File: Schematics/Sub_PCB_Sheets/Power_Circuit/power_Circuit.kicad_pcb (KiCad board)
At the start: 2 copper layers, 494.6 x 179.4 mm, 277 parts, among them IC1 F280049CPMSR, IC2 CP2102N-A02-GQFN24R, IC3 TPD2EUSB30ADRTR, J1 23AH8786-Red, J10 464379202, J11 464369202, J12 464379202, J13 43045-1212, J14 43650-0418, J15 43650-0418, J16 464369202, J17 464379202, J18 43650-0418, J19 FTSH-105-01-LM-D-K, J2 23AH8785-Black, J20 43045-1212, J21 43650-0418, J22 43650-0418, J23 464369202, J24 43650-0418, J25 43650-0418, J26 43650-0418, J27 43650-0418, J28 1051330011, J3 23AH8786-Red, J4 23AH8785-Black, J5 464379202, J6 464369202, J7 43650-0418, J8 464379202, J9 464369202, Q1 STB10NK60ZT4, Q2 C3M0025065K, Q3 C3M0025065K, Q4 C3M0025065K, Q5 C3M0025065K, Q6 PC817X1CSP9F, Q7 PC817X1CSP9F, Q8 STB10NK60ZT4, U1 UCC21710QDWRQ1, U2 UCC21710QDWRQ1, U3 UCC21710QDWRQ1, U4 UCC21710QDWRQ1, U5 TR05S3V3, Y1 ABM8-20.000MHZ-B2-T

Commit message: Power Board PCB completed and generated Feb output files
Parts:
- removed C1: 1 uF, SiC_Inverter:R71PI410050H6K
- removed C10, C12, C14, C15, C16, C2, C3, C4, C6, C8: 22 uF, SiC_Inverter:ESH226M500AL4AA
- removed C11, C13, C5, C7, C9: 2 uF, SiC_Inverter:MKP1848C52050JK2
- removed C17, C18, C35, C36: 15 uF, Capacitor_SMD:C_1206_3216Metric_Pad1.33x1.80mm_HandSolder
- removed C19, C20, C26, C29, C30, C33, C37, C38, C44, C47, C48, C51, C54, C55, C56, C57, C58, C60, C61, C62, C63, C66, C67: 0.1 uF, Capacitor_SMD:C_0805_2012Metric_Pad1.18x1.45mm_HandSolder
- removed C21, C22, C27, C34, C39, C40, C45, C52, C69: 1 uF, Capacitor_SMD:C_1206_3216Metric_Pad1.33x1.80mm_HandSolder
- removed C23, C24, C25, C28, C31, C32, C41, C42, C43, C46, C49, C50: 100 pF, Capacitor_SMD:C_0603_1608Metric_Pad1.08x0.95mm_HandSolder
- removed C53: 6.8 uF, SiC_Inverter:C4AF9BW4680T3FK
- removed C59, C68: 10 uF, Capacitor_SMD:C_0805_2012Metric_Pad1.18x1.45mm_HandSolder
- removed C64, C65: 18 pF, Capacitor_SMD:C_0402_1005Metric_Pad0.74x0.62mm_HandSolder
- removed D1, D7: BZX84C15-7-F, Package_TO_SOT_SMD:SOT-23-3
- removed D2, D3, D4, D5: BZX84C20-7-F, Package_TO_SOT_SMD:SOT-23-3
- removed D6: P6KE500A-HF, Diode_THT:D_DO-15_P12.70mm_Horizontal
- removed F1: 0031.8322, SiC_Inverter:0031.8322
- removed the G*** at (500.1, 162.0)
- removed the G*** at (67.5, 176.0)
- removed the G*** at (153.3, 177.6)
- removed the G*** at (299.4, 164.9)
- removed the G*** at (224.0, 180.9)
- removed the G*** at (382.6, 134.4)
- removed the G*** at (299.1, 62.0)
- removed H1, H13, H14, H15, H16, H17, H18, H19, H2, H20, H21, H22, H23, H24, H25, H26, H27, H28, H29, H3, H30, H31, H32, H4, H5, H6, H7, H8: MountingHole, MountingHole:MountingHole_2.2mm_M2
- removed IC1: F280049CPMSR, SiC_Inverter:F280049CPMSR
- removed IC2: CP2102N-A02-GQFN24R, SiC_Inverter:CP2102N-A02-GQFN24R
- removed IC3: TPD2EUSB30ADRTR, SiC_Inverter:TPD2EUSB30ADRTR
- removed J1, J3: 23AH8786-Red, SiC_Inverter:23AH8786-Red
- removed J10, J12, J17, J5, J8: 464379202, SiC_Inverter:46437-900_02
- removed J11, J16, J23, J6, J9: 464369202, SiC_Inverter:46436-900_02
- removed J13, J20: 43045-1212, SiC_Inverter:43045-1212
- removed J14, J15, J18, J21, J22, J24, J7: 43650-0418, SiC_Inverter:436500418
- removed J19: FTSH-105-01-LM-D-K, SiC_Inverter:FTSH-105-01-LM-D-K
- removed J2, J4: 23AH8785-Black, SiC_Inverter:23AH8785-Black
- removed J28: 1051330011, SiC_Inverter:105133-0011
- removed L1: 47 uH, SiC_Inverter:2300HT_470
- removed L2: 2.2 mH, SiC_Inverter:7448258022
- removed L3, L4: 470 uH, SiC_Inverter:1140471KRC
- removed Q1, Q8: STB10NK60ZT4, Package_TO_SOT_SMD:TO-263-2
- removed Q2, Q3, Q4, Q5: C3M0025065K, SiC_Inverter:C3M0025065K
- removed Q6, Q7: PC817X1CSP9F, SiC_Inverter:PC817X1CSP9F
- removed R1, R44, R45: 499 K, Resistor_SMD:R_1206_3216Metric_Pad1.30x1.75mm_HandSolder
- removed R10, R21, R22, R23, R24, R7, R8, R9: 10, Resistor_SMD:R_1206_3216Metric_Pad1.30x1.75mm_HandSolder
- removed R11, R13, R14, R16, R17, R18, R25, R27, R28, R30, R31, R32: 5 K, Resistor_SMD:R_1206_3216Metric_Pad1.30x1.75mm_HandSolder
- removed R12, R15, R26, R29: 100, Resistor_SMD:R_1206_3216Metric_Pad1.30x1.75mm_HandSolder
- removed R19, R20, R34, R36, R37, R39, R4, R40, R41, R43, R47, R48, R5, R6: 100 K, Resistor_SMD:R_1206_3216Metric_Pad1.30x1.75mm_HandSolder
- removed R2: CW005100R0JE12HE, SiC_Inverter:CW005100R0JE12HE
- removed R3, R46: 47, Resistor_SMD:R_1206_3216Metric_Pad1.30x1.75mm_HandSolder
- removed R33: 6, SiC_Inverter:CW005100R0JE12HE
- removed R35, R42: 10 K, Resistor_SMD:R_1206_3216Metric_Pad1.30x1.75mm_HandSolder
- removed R38: 2 K, Resistor_SMD:R_1206_3216Metric_Pad1.30x1.75mm_HandSolder
- removed R49: 0, Resistor_SMD:R_1206_3216Metric_Pad1.30x1.75mm_HandSolder
- removed TP1, TP11, TP24, TP25, TP26, TP27, TP3, TP32, TP34, TP35, TP36, TP37, TP38, TP40, TP41, TP42, TP43, TP44, TP45, TP46, TP47, TP48, TP49, TP5, TP50, TP51, TP52, TP53, TP54, TP55, TP56, TP57, TP58, TP60, TP61, TP62, TP63, TP64, TP65, TP67, TP69, TP7, TP8: 5277, SiC_Inverter:5277
- removed TP10, TP2, TP33, TP39, TP4, TP59, TP6, TP66, TP68, TP76, TP9: 5281, SiC_Inverter:5281
- removed U1, U2, U3, U4: UCC21710QDWRQ1, SiC_Inverter:UCC21710QDWRQ1
- removed Y1: ABM8-20.000MHZ-B2-T, SiC_Inverter:ABM8-20.000MHZ-B2-T
- moved TP71 10.0 mm to (161.4, 70.0)
- moved TP72 10.0 mm to (142.9, 70.2)
- moved TP74 10.0 mm to (152.1, 70.2)
- moved H10 9.00 mm to (111.6, 117.0)
- moved H11 9.00 mm to (185.1, 71.0)
- moved H12 9.00 mm to (184.9, 117.0)
- moved H9 9.00 mm to (111.6, 71.0)
- moved J25 9.00 mm to (130.4, 116.8)
- moved J26 9.00 mm to (183.9, 88.5)
- moved J27 9.00 mm to (175.7, 116.8)
- moved PS1 9.00 mm to (126.6, 91.2)
- moved PS2 9.00 mm to (158.6, 97.5)
- moved TP70 9.00 mm to (161.4, 77.5)
- moved TP73 9.00 mm to (142.9, 77.5)
- moved TP75 9.00 mm to (152.1, 77.5)
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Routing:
- net LOGIC_GND: track 232.6 -> 27.9 mm, vias 36 -> 0
- net GND: track 192.5 -> 7.93 mm, vias 24 -> 0
- net +3V3: track 194.4 -> 39.9 mm, vias 32 -> 0
- net /Con_PWM_A_H: track 116.7 -> 0.00 mm, vias 1 -> 0
- net /Con_PWM_A_L: track 104.9 -> 0.00 mm, vias 1 -> 0
- net /Con_EN_B_H: track 104.7 -> 0.00 mm, vias 1 -> 0
- net /Con_PWM_B_H: track 97.3 -> 0.00 mm, vias 1 -> 0
- net /Con_PWM_B_L: track 92.3 -> 0.00 mm, vias 1 -> 0
- net /Con_EN_A_L: track 91.9 -> 0.00 mm, vias 1 -> 0
- net /Con_FLT_B_H: track 88.3 -> 0.00 mm, vias 1 -> 0
- net /Con_RDY_A_H: track 85.5 -> 0.00 mm, vias 1 -> 0
- net /Con_FLT_B_L: track 81.8 -> 0.00 mm, vias 1 -> 0
- net /Con_RDY_A_L: track 79.6 -> 0.00 mm, vias 1 -> 0
- net /Con_FLT_A_L: track 76.6 -> 0.00 mm, vias 1 -> 0
- net /Controller/XRSn: track 68.3 -> 0.00 mm, vias 1 -> 0
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- removed copper zone on B.Cu, net +3V3
- removed copper zone on F.Cu, net +VIN
- removed copper zone on F.Cu, net -VIN
- removed copper zone on F.Cu, net /DC_Link_Caps/BUS_DC+
- removed copper zone on F.Cu, net /EMI_Input_Filter/BUS+_Filtered
- removed copper zone on F.Cu, net /EMI_Input_Filter/BUS+_RAW
- removed copper zone on F.Cu, net /Phase_A_Output
- removed copper zone on B.Cu, net /Phase_B_Output
- removed copper zone on B.Cu, net GND_ISO_LAHS
- removed copper zone on F.Cu, net GND_ISO_LBHS
- removed copper zone on B.Cu, net LOGIC_GND
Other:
- board size 494.6 x 179.4 mm -> 83 x 57 mm
- board text removed: "(325-425) VDC Input"
- board text removed: "+DC Filtered"
- board text removed: "+DC_BUS"
- board text removed: "+VIN"
- board text removed: "+VIN_Pro"
- board text removed: "-VIN"
- board text removed: "120Vrms Single Phase L-L"
- board text removed: "2.08 Inches"
- board text removed: "AC Output Filter"
- board text removed: "CPro G_Node"
- board text removed: "Controller + USB"
- board text removed: "DC Input / Protection Circuit"
- board text removed: "DC Input and Input Protection Circuit"
- board text removed: "DC Link Caps"
- board text removed: "DC+"
- board text removed: "EMI Input Filter"
- board text removed: "EN_AH"
- board text removed: "EN_AL"
- board text removed: "EN_BH"
- board text removed: "EN_BL"
- board text removed: "FLT_AH"
- board text removed: "FLT_AL"
- board text removed: "FLT_BH"
- board text removed: "FLT_BL"
- board text removed: "Full-Bridge"
- board text removed: "GND"
- board text removed: "G_Node"
- board text removed: "HS_Gate"
- board text removed: "High Side"
- board text removed: "J-TAG"
- board text removed: "LS_Gate"
- board text removed: "Leg A"
- board text removed: "Leg B"
- board text removed: "Logic GND"
- board text removed: "Low Side"
- board text removed: "Need to move to a 4 layer board when on its own PCB sheet"
- board text removed: "Open Loop Design"
- board text removed: "PWM AH"
- board text removed: "PWM AL"
- board text removed: "PWM BH"
- board text removed: "PWM BL"
- board text removed: "PWM_A_H"
- board text removed: "PWM_A_L"
- board text removed: "PWM_B_H"
- board text removed: "PWM_B_L"
- board text removed: "Phase A Node"
- board text removed: "Phase A Output"
- board text removed: "Phase B Node"
- board text removed: "Phase B Output"
- board text removed: "Pre G_Node"
- board text removed: "Pre-Charge Circuit"
- board text removed: "Pre-Charge_Current_Limiting"
- board text removed: "Pro G_Node"
- board text removed: "RDY_AH"
- board text removed: "RDY_AL"
- board text removed: "RDY_BH"
- board text removed: "RDY_BL"
- board text removed: "SiC Full Bridge"
- board text removed: "SiC Single Phase Inverter Controller"
- board text removed: "TCK"
- board text removed: "TDI"
- board text removed: "TDO"
- board text removed: "TMS"
- board text removed: "To Controller J20"
- board text removed: "To Controller J21"
- board text removed: "To Controller J22"
- board text removed: "To Full-Bridge J13"
- board text removed: "To Full-Bridge J14"
- board text removed: "To Power Board J25"
- board text removed: "To Power J26"
- board text removed: "To Power J27"
- board text removed: "To Pre-Charge J7"
- board text removed: "X1"
- board text removed: "X2"
- board text removed: "XRS"

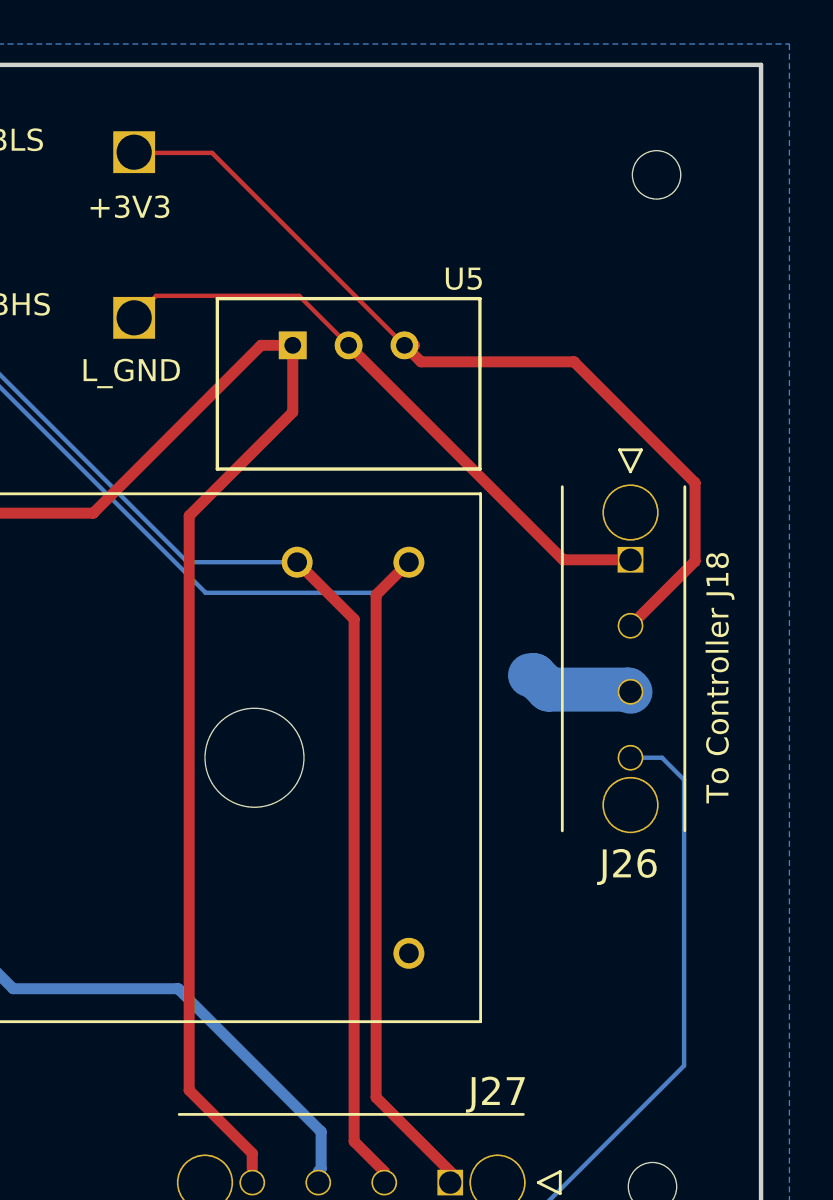
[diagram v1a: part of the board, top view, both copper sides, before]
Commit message: Added J30 to the Power Board and new Fab output
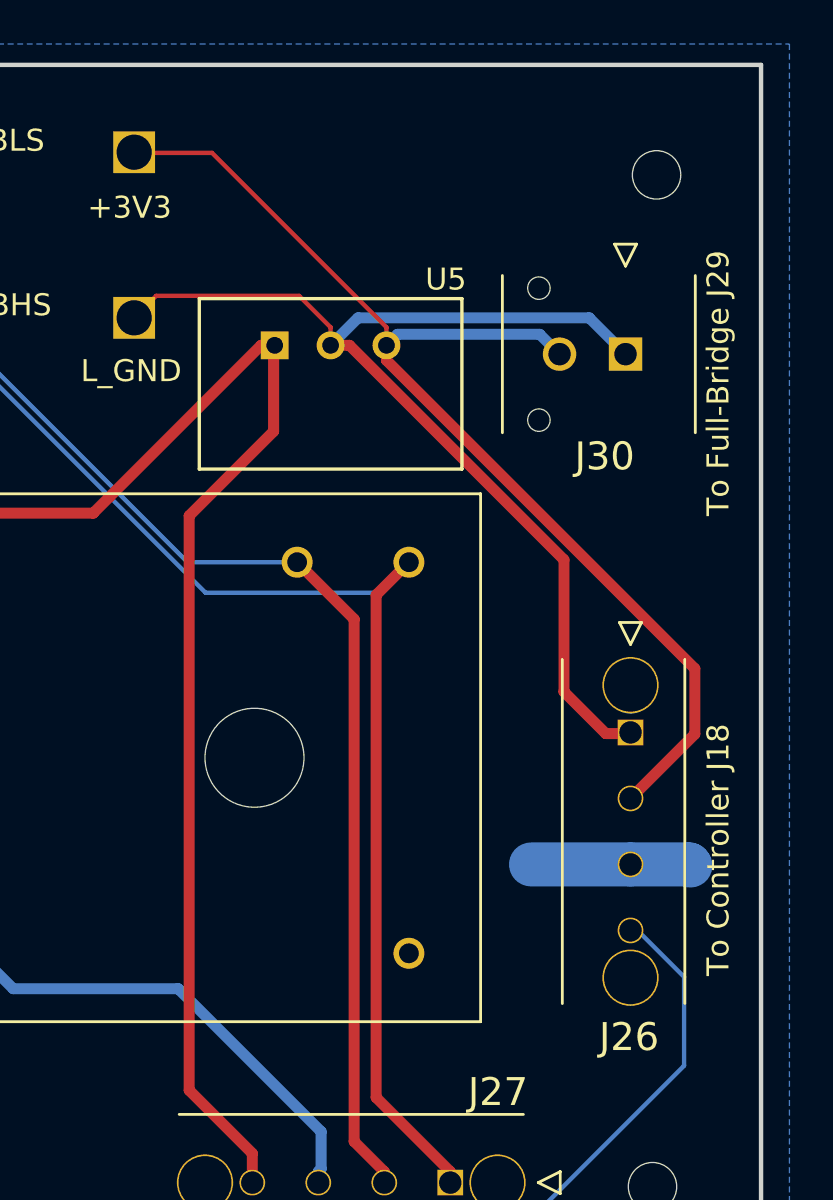
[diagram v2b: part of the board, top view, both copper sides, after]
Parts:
- added J30: 43045-0212, SiC_Inverter:43045-0212, F.Cu at (183.7, 79.2)
- moved J26 7.85 mm to (183.9, 96.3)
- moved U5 0.82 mm to (167.8, 78.8)
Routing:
- net LOGIC_GND: track 27.9 -> 49.8 mm
- net +3V3: track 39.9 -> 51.7 mm
- net /Con_Pro_Gate_node_output: track 86.9 -> 78.4 mm
- net GND: track 7.93 -> 10.5 mm
- net +15V_ISO_LALS: track 134.0 -> 132.8 mm
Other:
- board text added: "To Full-Bridge J29"
